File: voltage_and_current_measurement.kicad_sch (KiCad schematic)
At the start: 86 parts, among them IC2 VIA2000SD, J5 V_bat_in, J6 V_bat_out, J7 V_bat_in, J8 V_bat_out, U2 ACS37030LLZATR-065B3, U3 CZ3A05, U4 OPA2328DR, U5 OPA2328DR

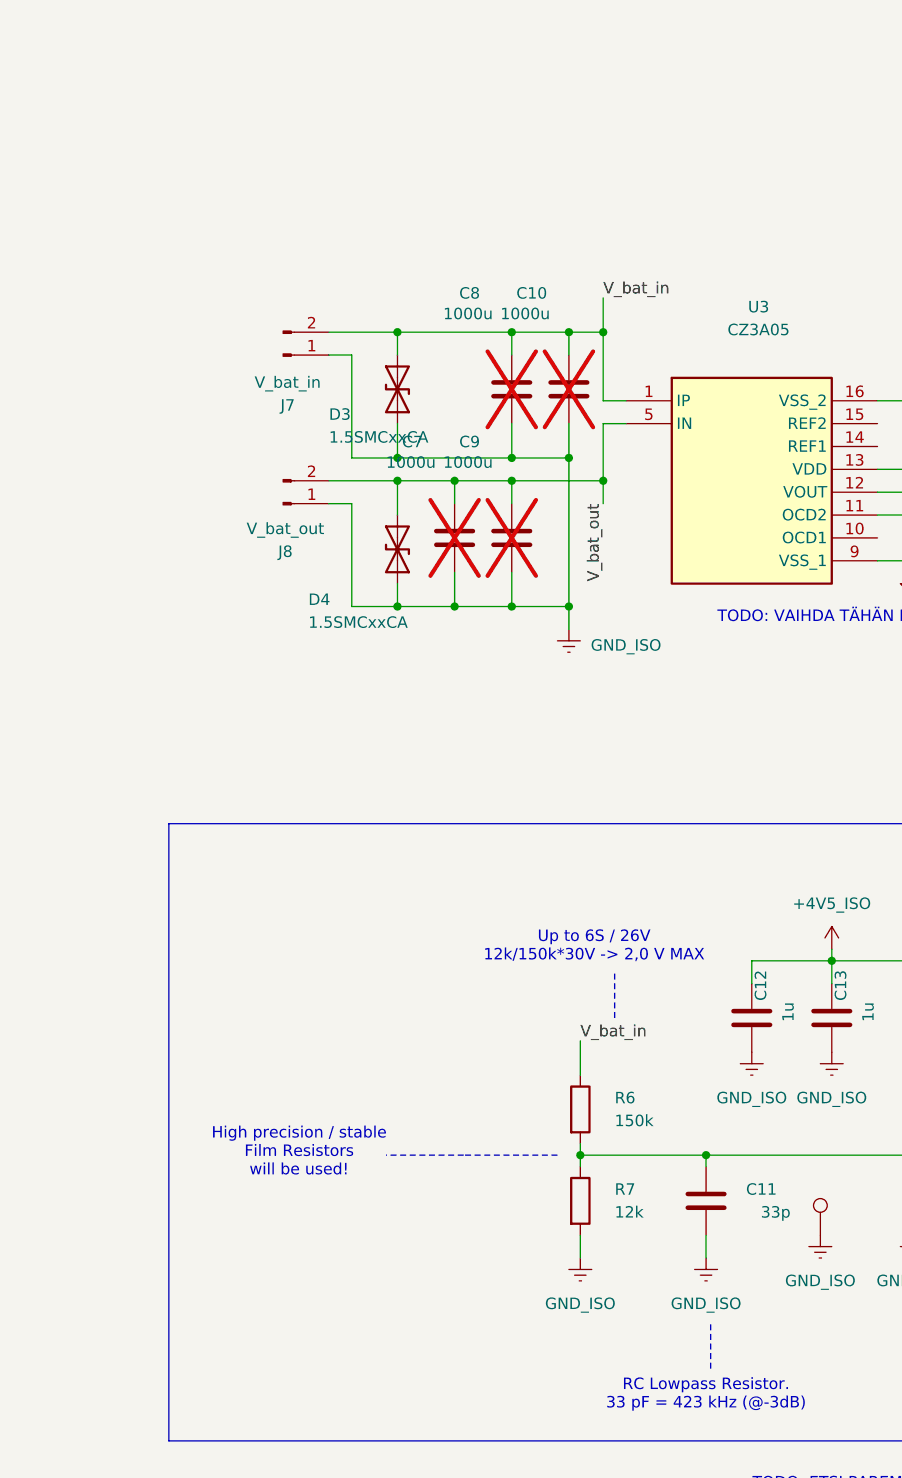
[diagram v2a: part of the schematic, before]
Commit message: Add Kelvin voltage measurement.
[KiCad Version: 10.0.4]
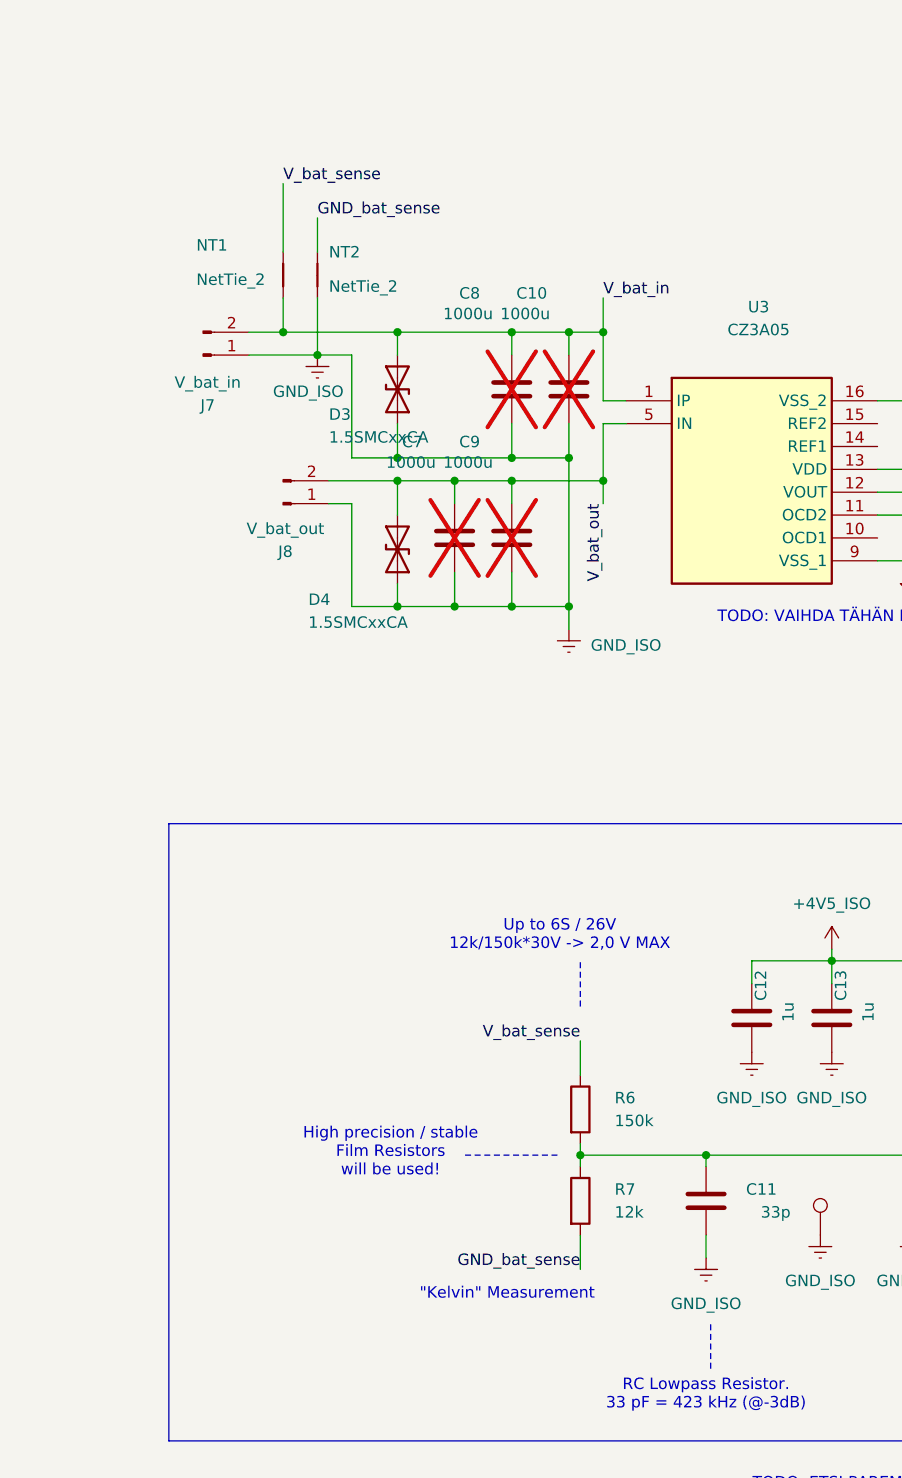
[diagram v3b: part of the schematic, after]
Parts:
- added NT1, NT2: NetTie_2, NetTie:NetTie-2_SMD_Pad0.5mm, symbol Device:NetTie_2
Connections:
- net GND_ISO: now also NT2.1; no longer R7.2
- net V_bat_in: now also NT1.1; no longer R6.1
- new net GND_bat_sense: NT2.2, R7.2
- new net V_bat_sense: NT1.2, R6.1
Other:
- note added: ""Kelvin" Measurement"
- moved on the sheet: J7

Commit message: Minor Tweaks.
[KiCad Version: 10.0.4]
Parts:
- renumbered C9 to C10, C10 to C11, C11 to C12, C12 to C13, C13 to C14, C14 to C15, C15 to C16, C16 to C17, C17 to C18, C18 to C19, C19 to C20, C20 to C21, C21 to C22, C22 to C23, C23 to C24, C24 to C25, C25 to C26, C26 to C27, C27 to C28, C28 to C29, C2 to C3, C29 to C30, C30 to C31, C31 to C32, C32 to C33, C33 to C34, C34 to C35, C35 to C36, C36 to C37, C37 to C38, C38 to C39, C3 to C4, C39 to C40, C40 to C41, C41 to C42, C42 to C43, C4 to C5, C5 to C6, C6 to C7, C7 to C8, C8 to C9

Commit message: Add Secondary battery voltage measurement. Minor tweaks.
[KiCad Version: 10.0.4]
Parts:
- renumbered C9 to C10, C10 to C11, C11 to C12, C12 to C13, C13 to C14, C14 to C15, C15 to C16, C16 to C17, C17 to C18, C18 to C19, C19 to C20, C20 to C21, C21 to C22, C22 to C23, C23 to C24, C24 to C25, C25 to C26, C26 to C27, C27 to C28, C28 to C29, C29 to C30, C30 to C31, C31 to C32, C32 to C33, C33 to C34, C34 to C35, C35 to C36, C36 to C37, C37 to C38, C38 to C39, C3 to C4, C39 to C40, C40 to C41, C41 to C42, C42 to C43, C43 to C44, C4 to C5, C5 to C6, C6 to C7, C7 to C8, C8 to C9, R8 to R10, R9 to R11, R10 to R12, R11 to R13, R12 to R14, R13 to R15, R14 to R16, R15 to R17, R16 to R18, R17 to R19, R18 to R20, R19 to R21, R20 to R22, R21 to R23, R6 to R8, R7 to R9

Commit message: Commit before complete rework for ESP32S3Module
[KiCad Version: 10.0.4]
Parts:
- renumbered U2 to U3, U3 to U4, U4 to U5, U5 to U6
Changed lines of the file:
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@@
 		(in_pos_files yes)
 		(dnp no)
-		(property "Reference" "U3"
+		(property "Reference" "U4"
 			(at 83.312 72.136 0)
 			(show_name no)
@@
 			(project "motor_testbench_v1_0"
 				(path "/da638649-102c-44f9-b928-e91cd399cc2f/2da1fd24-7545-4e4a-b589-72e0f66a31f4"
-					(reference "U3")
+					(reference "U4")
 					(unit 1)
 				)
@@
 		(dnp no)
 		(fields_autoplaced yes)
-		(property "Reference" "U5"
+		(property "Reference" "U6"
 			(at 238.76 134.62 0)
 			(show_name no)
@@
 			(project "motor_testbench_v1_0"
 				(path "/da638649-102c-44f9-b928-e91cd399cc2f/2da1fd24-7545-4e4a-b589-72e0f66a31f4"
-					(reference "U5")
+					(reference "U6")
 					(unit 1)
 				)
@@
 		(dnp no)
 		(fields_autoplaced yes)
-		(property "Reference" "U4"
+		(property "Reference" "U5"
 			(at 339.09 224.7899 0)
 			(show_name no)
@@
 			(project "motor_testbench_v1_0"
 				(path "/da638649-102c-44f9-b928-e91cd399cc2f/2da1fd24-7545-4e4a-b589-72e0f66a31f4"
-					(reference "U4")
+					(reference "U5")
 					(unit 3)
 				)
@@
 		(dnp no)
 		(fields_autoplaced yes)
-		(property "Reference" "U5"
+		(property "Reference" "U6"
 			(at 238.76 168.91 0)
 			(show_name no)
@@
 			(project "motor_testbench_v1_0"
 				(path "/da638649-102c-44f9-b928-e91cd399cc2f/2da1fd24-7545-4e4a-b589-72e0f66a31f4"
-					(reference "U5")
+					(reference "U6")
 					(unit 2)
 				)
@@
 		(dnp no)
 		(fields_autoplaced yes)
-		(property "Reference" "U4"
+		(property "Reference" "U5"
 			(at 238.76 90.17 0)
 			(show_name no)
@@
 			(project "motor_testbench_v1_0"
 				(path "/da638649-102c-44f9-b928-e91cd399cc2f/2da1fd24-7545-4e4a-b589-72e0f66a31f4"
-					(reference "U4")
+					(reference "U5")
 					(unit 2)
 				)
@@
 		(in_pos_files yes)
 		(dnp no)
-		(property "Reference" "U2"
+		(property "Reference" "U3"
 			(at -48.006 68.58 0)
 			(show_name no)
@@
 			(project "motor_testbench_v1_0"
 				(path "/da638649-102c-44f9-b928-e91cd399cc2f/2da1fd24-7545-4e4a-b589-72e0f66a31f4"
-					(reference "U2")
+					(reference "U3")
 					(unit 1)
 				)
@@
 		(dnp no)
 		(fields_autoplaced yes)
-		(property "Reference" "U5"
+		(property "Reference" "U6"
 			(at 355.6 224.7899 0)
 			(show_name no)
@@
 			(project "motor_testbench_v1_0"
 				(path "/da638649-102c-44f9-b928-e91cd399cc2f/2da1fd24-7545-4e4a-b589-72e0f66a31f4"
-					(reference "U5")
+					(reference "U6")
 					(unit 3)
 				)
@@
 		(dnp no)
 		(fields_autoplaced yes)
-		(property "Reference" "U4"
+		(property "Reference" "U5"
 			(at 238.76 55.88 0)
 			(show_name no)
@@
 			(project "motor_testbench_v1_0"
 				(path "/da638649-102c-44f9-b928-e91cd399cc2f/2da1fd24-7545-4e4a-b589-72e0f66a31f4"
-					(reference "U4")
+					(reference "U5")
 					(unit 1)
 				)

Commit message: Started implementing ESP32Module
[KiCad Version: 10.0.4]
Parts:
- renumbered J5 to J6, J6 to J7, J7 to J8, J8 to J9
